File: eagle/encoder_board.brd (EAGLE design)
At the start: 99.1 x 89 mm, 166 parts, among them CN1 6p-2.54, IC1 MEGA8-MI, IC2 AT42QT1010SOT23, X1 52745-0690, X2 52745-0690, X3 52745-0690, X4 POGOPIN-CONNWITHVIAS-SMV, X5 52745-0690

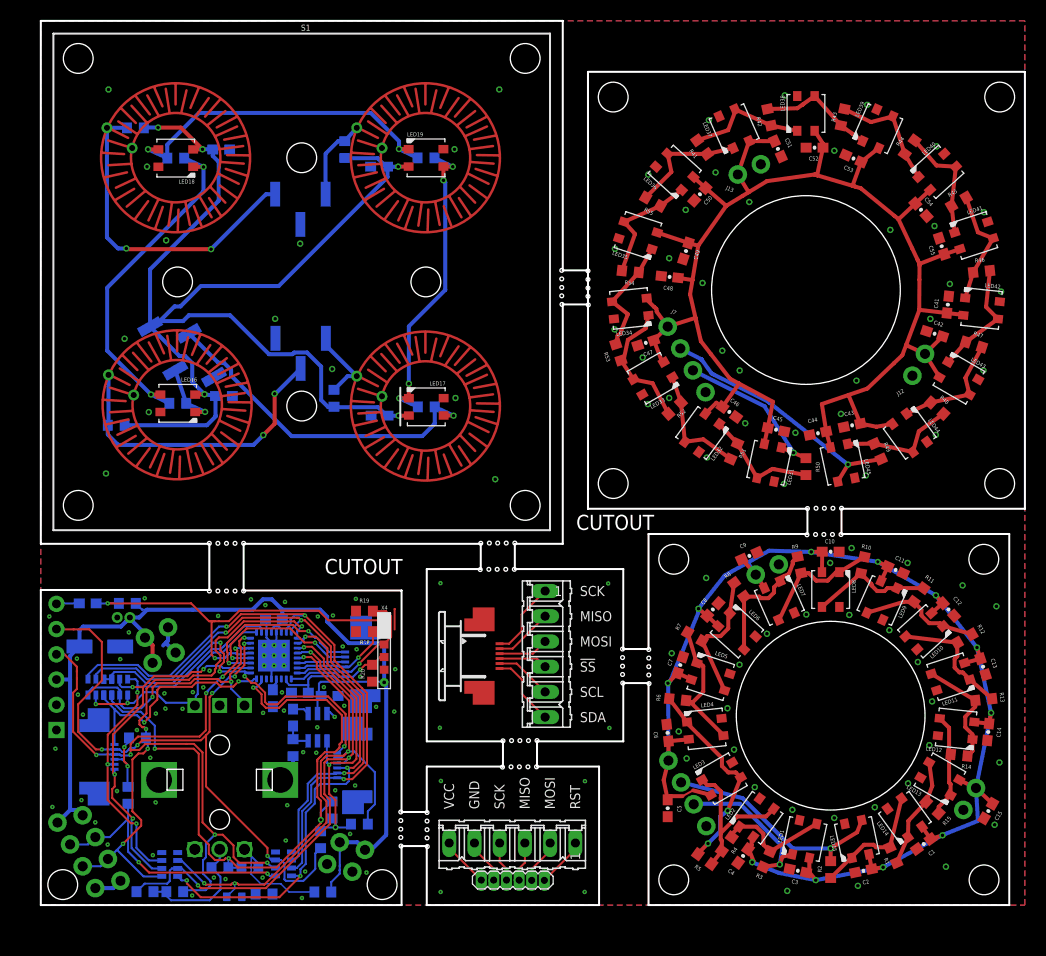
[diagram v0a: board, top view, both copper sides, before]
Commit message: Divide boards in design to separate files
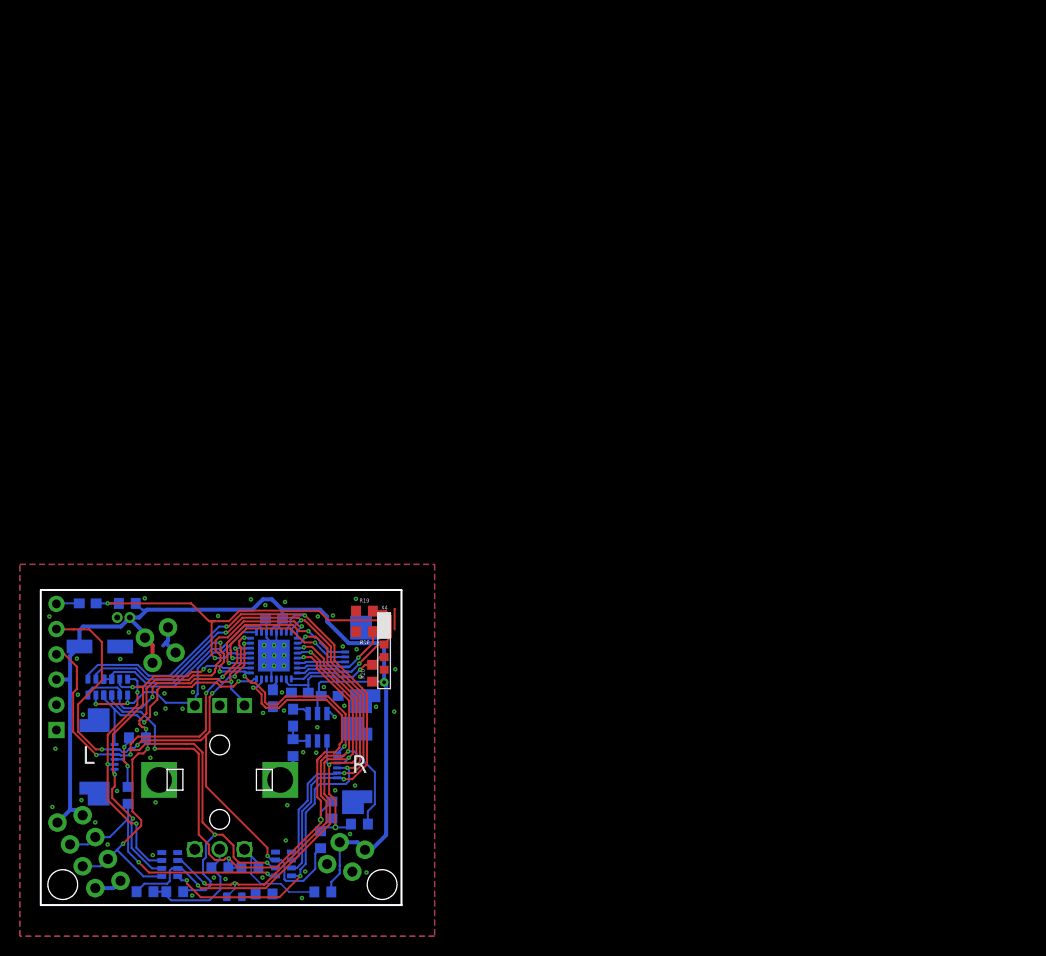
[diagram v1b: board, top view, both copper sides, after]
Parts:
- removed C1, C10, C11, C12, C13, C14, C15, C2, C20, C21, C22, C24, C3, C4, C41, C42, C43, C44, C45, C46, C47, C48, C49, C5, C50, C51, C52, C53, C54, C55, C6, C7, C8, C9: 100n, SparkFun-Capacitors:0603-CAP
- removed J1, J12, J13, J2: (no value), i2c_encoder:1X02_NO_SILK
- removed J3, J7: (no value), i2c_encoder:1X04_NO_SILK_ALL_ROUND
- removed JP1, JP2: (no value), pinhead_plus:1X03_SMT
- removed JP5: (no value), pinhead_plus:1X04_SMT
- removed LED1, LED10, LED11, LED12, LED13, LED14, LED15, LED16, LED17, LED18, LED19, LED2, LED3, LED31, LED32, LED33, LED34, LED35, LED36, LED37, LED38, LED39, LED4, LED40, LED41, LED42, LED43, LED44, LED45, LED5, LED6, LED7, LED8, LED9: WS2812B3535, i2c_encoder:LED3535
- removed R1, R10, R11, R12, R13, R14, R15, R2, R3, R4, R41, R42, R43, R44, R45, R46, R47, R48, R49, R5, R50, R51, R52, R53, R54, R55, R6, R7, R8, R9: (no value), rcl:R0603
- removed R26, R29, R30, R31: 0, rcl:R0603
- removed R32, R33, R34, R35: 10k, rcl:R0603
- removed S1: BUTTONPAD-2X2, i2c_encoder:BUTTONPAD-2X2-SINGLE
- removed SL1, SL2: (no value), con-amp-quick:06P
- removed U$1: 6PIN_1.27MM_POGO, i2c_encoder:1X06-1.27MM_POGO
- removed X5: 52745-0690, i2c_encoder:52745-0690
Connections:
- removed net N$1: LED10.3, LED11.1, R12.2, R13.1
- removed net N$10: LED8.3, LED9.1, R10.2, R11.1
- removed net N$11: LED3.3, LED4.1, R5.2, R6.1
- removed net N$12: LED14.3, LED15.1, R1.2, R2.1
- removed net N$13: LED16.3, LED18.1, R26.1, R30.1
- removed net N$14: LED1.3, LED2.1, R3.2, R4.1
- removed net N$16: LED42.3, LED43.1, R46.2, R47.1
- removed net N$17: LED4.3, LED5.1, R6.2, R7.1
- removed net N$18: LED5.3, LED6.1, R7.2, R8.1
- removed net N$19: LED6.3, LED7.1, R8.2, R9.1
- removed net N$2: LED11.3, LED12.1, R13.2, R14.1
- removed net N$20: LED43.3, LED44.1, R47.2, R48.1
- removed net N$21: LED44.3, LED45.1, R48.2, R49.1
- removed net N$22: LED10.1, LED9.3, R11.2, R12.1
- removed net N$23: LED32.3, LED33.1, R51.2, R52.1
- removed net N$24: LED33.3, LED34.1, R52.2, R53.1
- removed net N$25: LED34.3, LED35.1, R53.2, R54.1
- removed net N$26: LED35.3, LED36.1, R54.2, R55.1
- removed net N$27: LED7.3, LED8.1, R10.1, R9.2
- removed net N$28: LED31.3, LED32.1, R50.2, R51.1
- removed net N$29: LED40.3, LED41.1, R44.2, R45.1
- removed net N$3: LED37.3, LED38.1, R41.2, R42.1
- removed net N$30: LED41.3, LED42.1, R45.2, R46.1
- removed net N$4: LED38.3, LED39.1, R42.2, R43.1
- removed net N$43: LED17.1, LED19.3, R29.2, R31.1
- removed net N$44: LED18.3, LED19.1, R26.2, R29.1
- removed net N$46: LED36.3, LED37.1, R41.1, R55.2
- removed net N$5: LED2.3, LED3.1, R4.2, R5.1
- removed net N$6: LED13.3, LED14.1, R1.1, R15.2
- removed net N$8: LED39.3, LED40.1, R43.2, R44.1
- removed net N$9: LED12.3, LED13.1, R14.2, R15.1
- removed net RST: SL1.1, U$1.1
- net !SS: no longer SL2.4, X5.4
- net ENC1A: no longer JP2.1, R33.1, S1.SIG7
- net ENC1B: no longer JP2.3, R32.1, S1.SIG5
- net ENC_SW: no longer JP1.1, R35.1, S1.SIG3
- net GND: no longer C1.2, C10.2, C11.2, C12.2, C13.2, C14.2, C15.2, C2.2, C20.2, C21.2, C22.2, C24.2, C3.2, C4.2, C41.2, C42.2, C43.2, C44.2, C45.2, C46.2, C47.2, C48.2, C49.2, C5.2, C50.2, C51.2, C52.2, C53.2, C54.2, C55.2, C6.2, C7.2, C8.2, C9.2, J1.2, J12.2, J13.2, J2.2, J3.4, J7.4, JP1.3, JP2.2, JP5.4, LED1.4, LED10.4, LED11.4, LED12.4, LED13.4, LED14.4, LED15.4, LED16.4, LED17.4, LED18.4, LED19.4, LED2.4, LED3.4, LED31.4, LED32.4, LED33.4, LED34.4, LED35.4, LED36.4, LED37.4, LED38.4, LED39.4, LED4.4, LED40.4, LED41.4, LED42.4, LED43.4, LED44.4, LED45.4, LED5.4, LED6.4, LED7.4, LED8.4, LED9.4, S1.SIG2, S1.SIG4, S1.SIG6, S1.SIG8, SL1.5, U$1.5
- net LED1: no longer J3.3, J7.3, JP5.3, LED1.1, LED16.1, LED31.1, R3.1, R30.2, R50.1
- net LED_OUT: no longer J3.2, J7.2, JP5.2, LED15.3, LED17.3, LED45.3, R2.2, R31.2, R49.2
- net MISO: no longer SL1.3, SL2.2, U$1.3, X5.2
- net MOSI: no longer SL1.2, SL2.3, U$1.2, X5.3
- net POT: no longer JP1.2, R34.1, S1.SIG1
- net SCK: no longer SL1.4, SL2.1, U$1.4, X5.1
- net SCL: no longer SL2.5, X5.5
- net SDA: no longer SL2.6, X5.6
- net VCC: no longer C1.1, C10.1, C11.1, C12.1, C13.1, C14.1, C15.1, C2.1, C20.1, C21.1, C22.1, C24.1, C3.1, C4.1, C41.1, C42.1, C43.1, C44.1, C45.1, C46.1, C47.1, C48.1, C49.1, C5.1, C50.1, C51.1, C52.1, C53.1, C54.1, C55.1, C6.1, C7.1, C8.1, C9.1, J1.1, J12.1, J13.1, J2.1, J3.1, J7.1, JP5.1, LED1.2, LED10.2, LED11.2, LED12.2, LED13.2, LED14.2, LED15.2, LED16.2, LED17.2, LED18.2, LED19.2, LED2.2, LED3.2, LED31.2, LED32.2, LED33.2, LED34.2, LED35.2, LED36.2, LED37.2, LED38.2, LED39.2, LED4.2, LED40.2, LED41.2, LED42.2, LED43.2, LED44.2, LED45.2, LED5.2, LED6.2, LED7.2, LED8.2, LED9.2, R32.2, R33.2, R34.2, R35.2, SL1.6, U$1.6
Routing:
- net VCC: track 540.0 -> 116.5 mm, vias 17 -> 0
- net LED_OUT: track 111.5 -> 27.6 mm, vias 5 -> 2
- net LED1: track 90.9 -> 51.3 mm, vias 7 -> 4
- net N$13: track 34.9 -> 0.00 mm, vias 2 -> 0
- net N$44: track 34.2 -> 0.00 mm, vias 2 -> 0
- net ENC1B: track 56.8 -> 24.0 mm, vias 4 -> 2
- net POT: track 43.8 -> 12.5 mm, vias 2 -> 0
- net N$43: track 30.9 -> 0.00 mm, vias 4 -> 0
- net N$11: track 20.5 -> 0.00 mm, vias 2 -> 0
- net N$5: track 16.7 -> 0.00 mm
- net N$17: track 13.7 -> 0.00 mm
- net N$24: track 13.5 -> 0.00 mm
- net N$18: track 13.3 -> 0.00 mm
- net N$19: track 13.2 -> 0.00 mm
- net N$1: track 12.8 -> 0.00 mm
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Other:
- board size 99.1 x 89 mm -> 36.3 x 31.7 mm
- board text added: "RLB"
- board text removed: "!SS"
- board text removed: "(-0.1 -0.03)"
- board text removed: "(0.03 0.1)"
- board text removed: "(0.1 -0.03)"
- board text removed: "(c> 2 1.9)"
- board text removed: "BTN"
- board text removed: "CUTOUT"
- board text removed: "GND"
- board text removed: "MISO"
- board text removed: "MOSI"
- board text removed: "RST"
- board text removed: "SCK"
- board text removed: "SCL"
- board text removed: "SDA"
- board text removed: "Siirrä X3 ylemmäs?"
- board text removed: "VCC"
